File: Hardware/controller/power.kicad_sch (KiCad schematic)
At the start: 37 parts, among them J201 Screw_Terminal_01x03, U201 BD9D321EFJ, U202 MCP1703AT-5002E/DB, U203 ICL7660

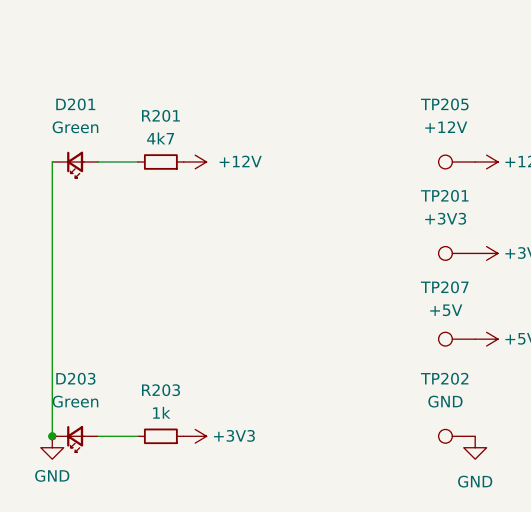
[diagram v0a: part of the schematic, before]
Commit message: Add +5V indicator
- Adds a LED to indicate the 5V supply is active
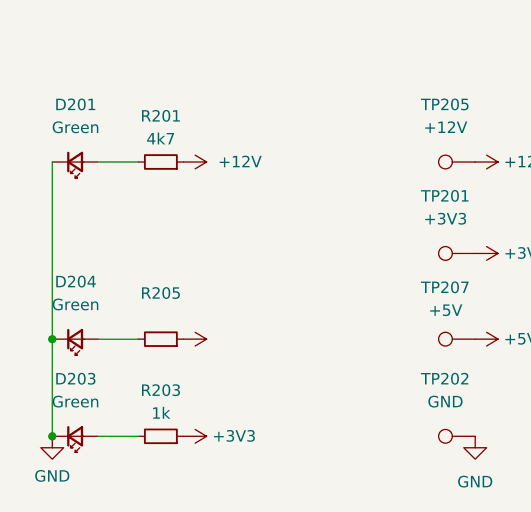
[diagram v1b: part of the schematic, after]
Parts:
- added D204: Green, LED_SMD:LED_0805_2012Metric_Pad1.15x1.40mm_HandSolder, symbol Device:LED_Small
- added R205: (no value), symbol Device:R_Small
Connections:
- net +5V: now also R205.1
- net GND: now also D204.1 (K)
- new net: D204.2 (A), R205.2
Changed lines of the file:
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@@
   (junction (at 52.07 35.56) (diameter 0) (color 0 0 0 0)
+  )
+  (junction (at 19.685 179.705) (diameter 0) (color 0 0 0 0)
   )
   (junction (at 117.475 38.1) (diameter 0) (color 0 0 0 0)
@@
     (stroke (width 0) (type default) (color 0 0 0 0))
   )
+  (wire (pts (xy 24.765 179.705) (xy 29.21 179.705))
+    (stroke (width 0) (type default) (color 0 0 0 0))
+  )
   (wire (pts (xy 187.96 142.24) (xy 187.96 143.51))
     (stroke (width 0) (type default) (color 0 0 0 0))
@@
     (stroke (width 0) (type default) (color 0 0 0 0))
   )
-  (wire (pts (xy 19.685 160.02) (xy 19.685 190.5))
+  (wire (pts (xy 19.685 160.02) (xy 19.685 179.705))
     (stroke (width 0) (type default) (color 0 0 0 0))
   )
@@
   )
   (wire (pts (xy 60.325 119.38) (xy 60.325 116.84))
+    (stroke (width 0) (type default) (color 0 0 0 0))
+  )
+  (wire (pts (xy 19.685 179.705) (xy 19.685 190.5))
     (stroke (width 0) (type default) (color 0 0 0 0))
   )
@@
     (pin "1")
   )
+  (symbol (lib_id "power:+5V") (at 34.29 179.705 270) (unit 1)
+    (in_bom yes) (on_board yes)
+    (property "Reference" "#PWR?" (id 0) (at 30.48 179.705 0)
+      (effects (font (size 1.27 1.27)) hide)
+    )
+    (property "Value" "" (id 1) (at 37.465 179.705 90)
+      (effects (font (size 1.27 1.27)) (justify left))
+    )
+    (property "Footprint" "" (id 2) (at 34.29 179.705 0)
+      (effects (font (size 1.27 1.27)) hide)
+    )
+    (property "Datasheet" "" (id 3) (at 34.29 179.705 0)
+      (effects (font (size 1.27 1.27)) hide)
+    )
+    (pin "1")
+  )
   (symbol (lib_id "power:NEUT") (at 273.05 148.59 180) (unit 1)
     (in_bom yes) (on_board yes)
@@
     )
     (pin "1")
+  )
+  (symbol (lib_id "Device:LED_Small") (at 22.225 179.705 0) (mirror x) (unit 1)
+    (in_bom yes) (on_board yes) (fields_autoplaced)
+    (property "Reference" "D204" (id 0) (at 22.2885 173.355 0))
+    (property "Value" "Green" (id 1) (at 22.2885 175.895 0))
+    (property "Footprint" "LED_SMD:LED_0805_2012Metric_Pad1.15x1.40mm_HandSolder" (id 2) (at 22.225 179.705 90)
+      (effects (font (size 1.27 1.27)) hide)
+    )
+    (property "Datasheet" "~" (id 3) (at 22.225 179.705 90)
+      (effects (font (size 1.27 1.27)) hide)
+    )
+    (property "MPN" "150080VS75000" (id 4) (at 22.225 179.705 0)
+      (effects (font (size 1.27 1.27)) hide)
+    )
+    (pin "1")
+    (pin "2")
   )
   (symbol (lib_id "power:NEUT") (at 264.16 115.57 90) (unit 1)
@@
       (effects (font (size 1.27 1.27)) hide)
     )
+    (pin "1")
+    (pin "2")
+  )
+  (symbol (lib_id "Device:R_Small") (at 31.75 179.705 270) (mirror x) (unit 1)
+    (in_bom yes) (on_board yes)
+    (property "Reference" "R205" (id 0) (at 31.75 174.625 90))
+    (property "Value" "" (id 1) (at 31.75 177.165 90))
+    (property "Footprint" "" (id 2) (at 31.75 179.705 0)
+      (effects (font (size 1.27 1.27)) hide)
+    )
+    (property "Datasheet" "~" (id 3) (at 31.75 179.705 0)
+      (effects (font (size 1.27 1.27)) hide)
+    )
+    (property "MPN" "RMC1/10-222JTP" (id 4) (at 31.75 179.705 90)
+      (effects (font (size 1.27 1.27)) hide)
+    )

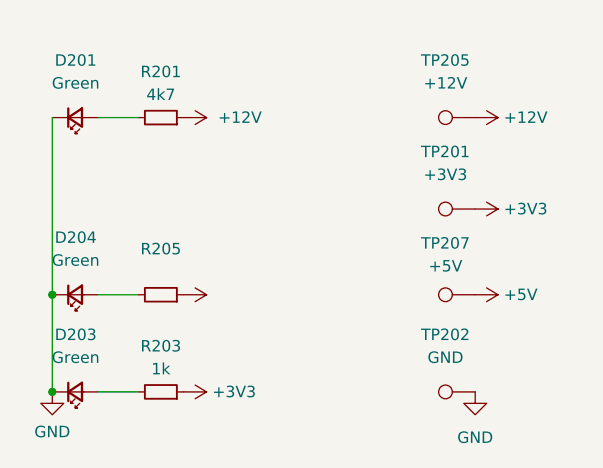
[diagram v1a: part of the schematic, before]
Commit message: Refactoring controller schematic
- Moved most of the connections out of the main sheet and into
  appropriate subsheets to increase the organization

- Updated analog board connection to have the SPI bus concept rather
  than a CAN bus; that way we don't need an additional micro on the
  analog board to drive things also

- Replaced latching connectors with regular shrouded headers
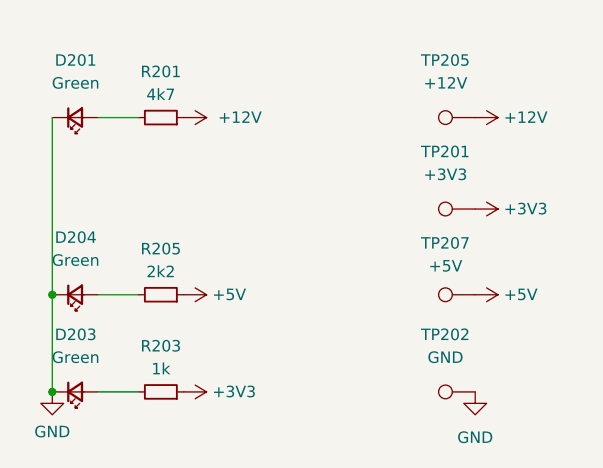
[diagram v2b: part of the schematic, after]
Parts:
- R205: value (none) -> 2k2; footprint (none) -> Resistor_SMD:R_0805_2012Metric_Pad1.20x1.40mm_HandSolder
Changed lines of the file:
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@@
   (symbol (lib_id "power:+5V") (at 34.29 179.705 270) (unit 1)
     (in_bom yes) (on_board yes)
-    (property "Reference" "#PWR?" (id 0) (at 30.48 179.705 0)
-      (effects (font (size 1.27 1.27)) hide)
-    )
-    (property "Value" "" (id 1) (at 37.465 179.705 90)
+    (property "Reference" "#PWR0227" (id 0) (at 30.48 179.705 0)
+      (effects (font (size 1.27 1.27)) hide)
+    )
+    (property "Value" "+5V" (id 1) (at 37.465 179.705 90)
       (effects (font (size 1.27 1.27)) (justify left))
     )
@@
     (in_bom yes) (on_board yes)
     (property "Reference" "R205" (id 0) (at 31.75 174.625 90))
-    (property "Value" "" (id 1) (at 31.75 177.165 90))
-    (property "Footprint" "" (id 2) (at 31.75 179.705 0)
-      (effects (font (size 1.27 1.27)) hide)
-    )
+    (property "Value" "2k2" (id 1) (at 31.75 177.165 90))
+    (property "Footprint" "Resistor_SMD:R_0805_2012Metric_Pad1.20x1.40mm_HandSolder" (id 2) (at 31.75 179.705 0)
+      (effects (font (size 1.27 1.27)) hide)
+    )

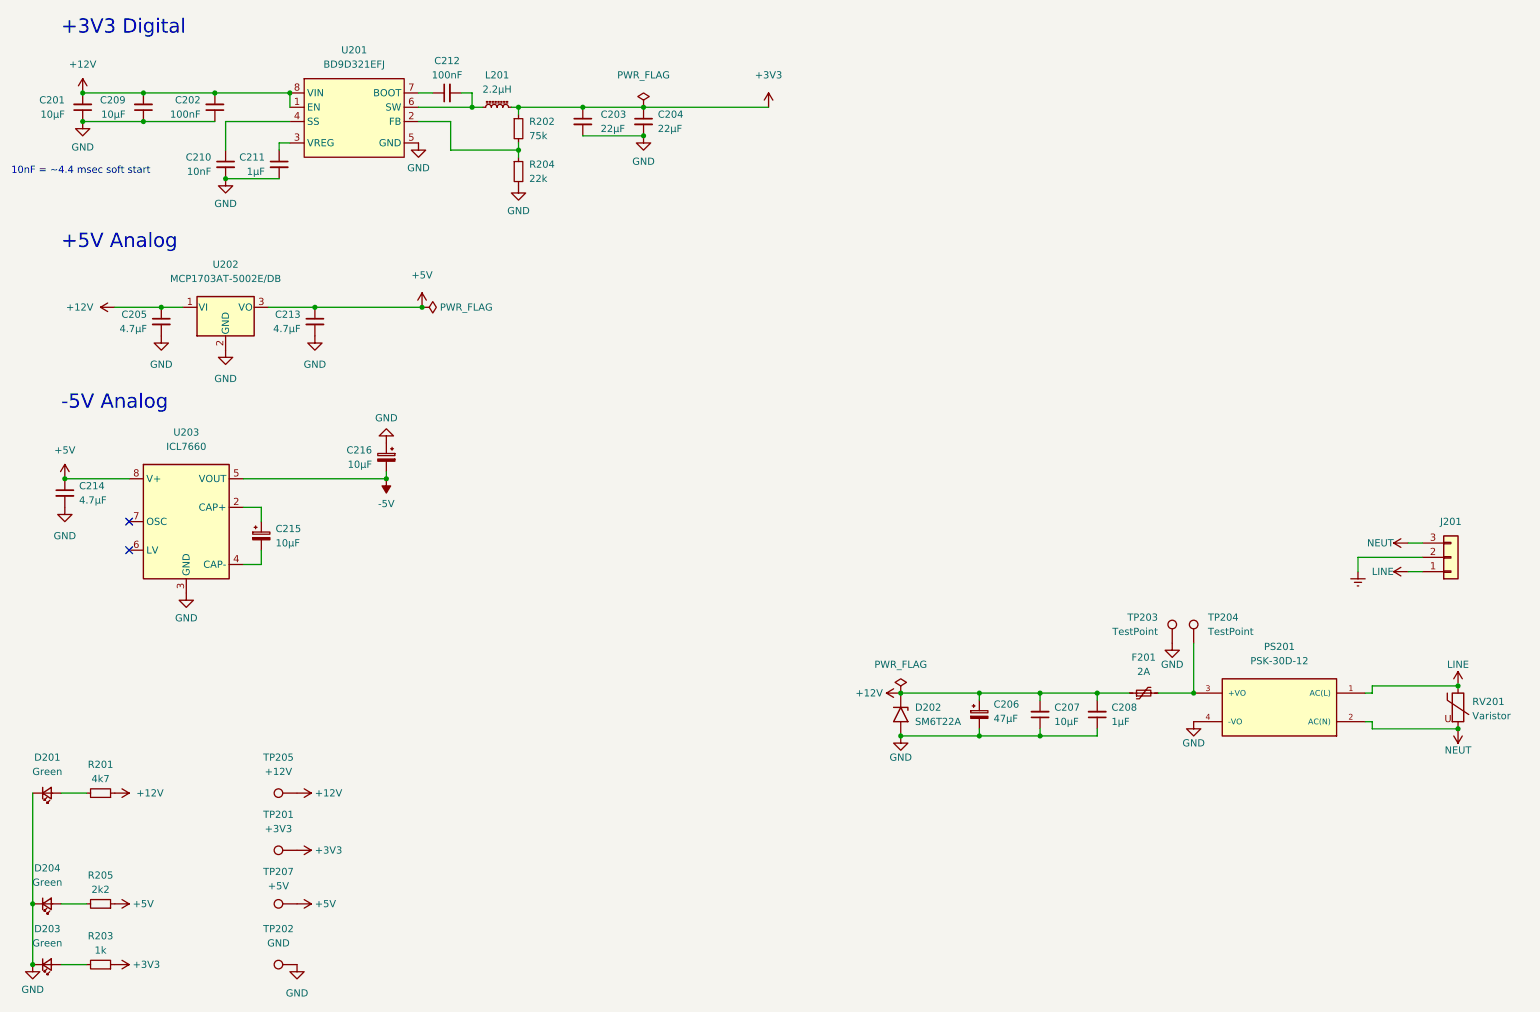
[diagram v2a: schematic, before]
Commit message: Cleaning up controller schematic/board
- This moves a few things around but doesn't functionally change
  anything; mostly this is moving the files to the KiCad nightly format
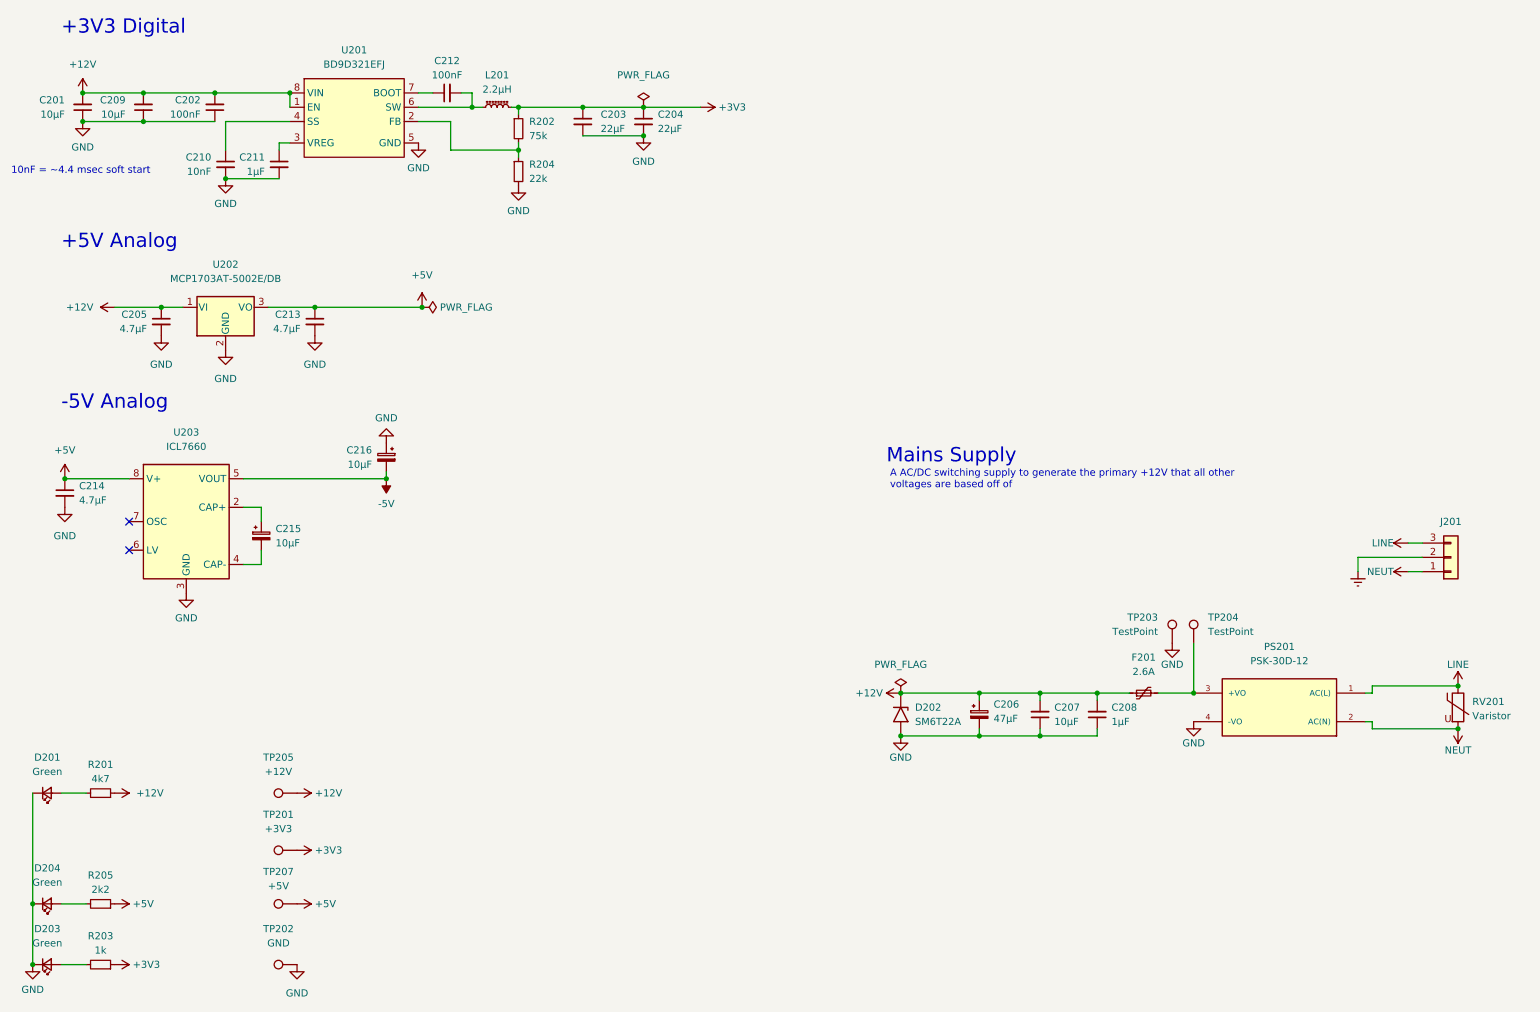
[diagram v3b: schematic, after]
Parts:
- F201: value 2A -> 2.6A; MPN 0ZCG0200AF2B -> 0ZCG0260BF2B
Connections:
- net LINE: now also J201.3 (Pin_3); no longer J201.1 (Pin_1)
- net NEUT: now also J201.1 (Pin_1); no longer J201.3 (Pin_3)
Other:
- note added: "A AC/DC switching supply to generate the primary +12V that all other voltages are based off of"
- note added: "Mains Supply"
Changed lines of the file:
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@@
+    (stroke (width 0) (type default) (color 0 0 0 0))
+  )
+  (wire (pts (xy 128.27 38.1) (xy 138.43 38.1))
     (stroke (width 0) (type default) (color 0 0 0 0))
   )
@@
   )
   (wire (pts (xy 24.765 190.5) (xy 29.21 190.5))
-    (stroke (width 0) (type default) (color 0 0 0 0))
-  )
-  (wire (pts (xy 128.27 38.1) (xy 150.495 38.1))
     (stroke (width 0) (type default) (color 0 0 0 0))
   )
@@
     (effects (font (size 2.54 2.54)) (justify left bottom))
   )
+  (text "A AC/DC switching supply to generate the primary +12V that all other\nvoltages are based off of"
+    (at 172.085 106.045 0)
+    (effects (font (size 1.27 1.27)) (justify left bottom))
+  )
   (text "-5V Analog" (at 24.765 92.075 0)
+    (effects (font (size 2.54 2.54)) (justify left bottom))
+  )
+  (text "Mains Supply" (at 171.45 101.6 0)
     (effects (font (size 2.54 2.54)) (justify left bottom))
   )
@@
     (pin "2")
   )
+  (symbol (lib_id "power:+3V3") (at 138.43 38.1 270) (unit 1)
+    (in_bom yes) (on_board yes)
+    (property "Reference" "#PWR0228" (id 0) (at 134.62 38.1 0)
+      (effects (font (size 1.27 1.27)) hide)
+    )
+    (property "Value" "+3V3" (id 1) (at 141.605 38.1 90)
+      (effects (font (size 1.27 1.27)) (justify left))
+    )
+    (property "Footprint" "" (id 2) (at 138.43 38.1 0)
+      (effects (font (size 1.27 1.27)) hide)
+    )
+    (property "Datasheet" "" (id 3) (at 138.43 38.1 0)
+      (effects (font (size 1.27 1.27)) hide)
+    )
+    (pin "1")
+  )
   (symbol (lib_id "power:GND") (at 88.265 44.45 0) (unit 1)
     (in_bom yes) (on_board yes) (fields_autoplaced)
@@
     (pin "2")
   )
-  (symbol (lib_id "power:NEUT") (at 264.16 115.57 90) (unit 1)
-    (in_bom yes) (on_board yes)
-    (property "Reference" "#PWR0208" (id 0) (at 267.97 115.57 0)
-      (effects (font (size 1.27 1.27)) hide)
-    )
-    (property "Value" "NEUT" (id 1) (at 261.62 115.57 90)
-      (effects (font (size 1.27 1.27)) (justify left))
-    )
-    (property "Footprint" "" (id 2) (at 264.16 115.57 0)
-      (effects (font (size 1.27 1.27)) hide)
-    )
-    (property "Datasheet" "" (id 3) (at 264.16 115.57 0)
+  (symbol (lib_id "power:NEUT") (at 264.16 120.65 90) (unit 1)
+    (in_bom yes) (on_board yes)
+    (property "Reference" "#PWR0208" (id 0) (at 267.97 120.65 0)
+      (effects (font (size 1.27 1.27)) hide)
+    )
+    (property "Value" "NEUT" (id 1) (at 261.62 120.65 90)
+      (effects (font (size 1.27 1.27)) (justify left))
+    )
+    (property "Footprint" "" (id 2) (at 264.16 120.65 0)
+      (effects (font (size 1.27 1.27)) hide)
+    )
+    (property "Datasheet" "" (id 3) (at 264.16 120.65 0)
       (effects (font (size 1.27 1.27)) hide)
     )
@@
     (pin "1")
   )
-  (symbol (lib_id "power:+3V3") (at 150.495 38.1 0) (unit 1)
-    (in_bom yes) (on_board yes) (fields_autoplaced)
-    (property "Reference" "#PWR0108" (id 0) (at 150.495 41.91 0)
-      (effects (font (size 1.27 1.27)) hide)
-    )
-    (property "Value" "+3V3" (id 1) (at 150.495 32.385 0))
-    (property "Footprint" "" (id 2) (at 150.495 38.1 0)
-      (effects (font (size 1.27 1.27)) hide)
-    )
-    (property "Datasheet" "" (id 3) (at 150.495 38.1 0)
-      (effects (font (size 1.27 1.27)) hide)
-    )
-    (pin "1")
-  )
   (symbol (lib_id "Device:C_Small") (at 63.5 48.26 0) (unit 1)
     (in_bom yes) (on_board yes)
@@
     (pin "2")
   )
+  (symbol (lib_id "Device:Polyfuse_Small") (at 217.17 142.24 90) (unit 1)
+    (in_bom yes) (on_board yes) (fields_autoplaced)
+    (property "Reference" "F201" (id 0) (at 217.17 135.89 90))
+    (property "Value" "2.6A" (id 1) (at 217.17 138.43 90))
+    (property "Footprint" "Fuse:Fuse_1812_4532Metric_Pad1.30x3.40mm_HandSolder" (id 2) (at 222.25 140.97 0)
+      (effects (font (size 1.27 1.27)) (justify left) hide)
+    )
+    (property "Datasheet" "~" (id 3) (at 217.17 142.24 0)
+      (effects (font (size 1.27 1.27)) hide)
+    )
+    (property "MPN" "0ZCG0260BF2B" (id 4) (at 217.17 142.24 90)
+      (effects (font (size 1.27 1.27)) hide)
+    )
+    (pin "1")
+    (pin "2")
+  )
   (symbol (lib_id "power:PWR_FLAG") (at 88.9 73.66 270) (mirror x) (unit 1)
     (in_bom yes) (on_board yes) (fields_autoplaced)
@@
     (pin "1")
   )
-  (symbol (lib_id "Device:Polyfuse_Small") (at 217.17 142.24 90) (unit 1)
-    (in_bom yes) (on_board yes) (fields_autoplaced)
-    (property "Reference" "F201" (id 0) (at 217.17 135.89 90))
-    (property "Value" "2A" (id 1) (at 217.17 138.43 90))
-    (property "Footprint" "Fuse:Fuse_1812_4532Metric_Pad1.30x3.40mm_HandSolder" (id 2) (at 222.25 140.97 0)
-      (effects (font (size 1.27 1.27)) (justify left) hide)
-    )
-    (property "Datasheet" "~" (id 3) (at 217.17 142.24 0)
-      (effects (font (size 1.27 1.27)) hide)
-    )
-    (property "MPN" "0ZCG0200AF2B" (id 4) (at 217.17 142.24 90)
-      (effects (font (size 1.27 1.27)) hide)
-    )
-    (pin "1")
-    (pin "2")
-  )
   (symbol (lib_id "power:GND") (at 42.545 78.74 0) (mirror y) (unit 1)
     (in_bom yes) (on_board yes) (fields_autoplaced)
@@
     (pin "1")
   )
-  (symbol (lib_id "power:LINE") (at 264.16 120.65 90) (unit 1)
-    (in_bom yes) (on_board yes)
-    (property "Reference" "#PWR0105" (id 0) (at 267.97 120.65 0)
-      (effects (font (size 1.27 1.27)) hide)
-    )
-    (property "Value" "LINE" (id 1) (at 261.62 120.65 90)
-      (effects (font (size 1.27 1.27)) (justify left))
-    )
-    (property "Footprint" "" (id 2) (at 264.16 120.65 0)
-      (effects (font (size 1.27 1.27)) hide)
-    )
-    (property "Datasheet" "" (id 3) (at 264.16 120.65 0)
-      (effects (font (size 1.27 1.27)) hide)
-    )
+  (symbol (lib_id "power:LINE") (at 264.16 115.57 90) (unit 1)
+    (in_bom yes) (on_board yes)
+    (property "Reference" "#PWR0105" (id 0) (at 267.97 115.57 0)
+      (effects (font (size 1.27 1.27)) hide)
+    )
+    (property "Value" "LINE" (id 1) (at 261.62 115.57 90)
+      (effects (font (size 1.27 1.27)) (justify left))
+    )
+    (property "Footprint" "" (id 2) (at 264.16 115.57 0)
+      (effects (font (size 1.27 1.27)) hide)
+    )
+    (property "Datasheet" "" (id 3) (at 264.16 115.57 0)
+      (effects (font (size 1.27 1.27)) hide)
+    )
